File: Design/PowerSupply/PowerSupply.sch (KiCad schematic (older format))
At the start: 14 parts, among them J1 Barrel_Jack, J2 Conn_01x02_Male, Q1 IRF644, U1 MAX1771

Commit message: Add part numbers to symbols in PowerSupply schematic for BOM
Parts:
- C1: Digikey # (none) -> 478-TPSD107M020R0150DKR-ND; Manufacturer (none) -> AVX
- C2, C3: Digikey # (none) -> 1276-1007-6-ND; Manufacturer (none) -> SAMSUNG
- C4: Digikey # (none) -> PCE3432DKR-ND; Manufacturer (none) -> PANASONIC
- D1: Digikey # (none) -> ES2F-E3/52TGIDKR-ND; Manufacturer (none) -> VISHAY
- J1: Digikey # (none) -> 2092-KLDX-0202-A-ND; Manufacturer (none) -> KYCON
- L1: Digikey # (none) -> 513-1526-6-ND; Manufacturer (none) -> EATON
- Q1: Digikey # (none) -> IRF644STRLPBFDKR-ND; Manufacturer (none) -> VISHAY
- R1: Digikey # (none) -> YAG2156DKR-ND; Manufacturer (none) -> YAGEO
- R2: Digikey # (none) -> 311-1.2MERDKR-ND; Manufacturer (none) -> YAGEO
- R3: Digikey # (none) -> 311-10KARDKR-ND; Manufacturer (none) -> YAGEO
- RV1: Digikey # (none) -> 3362P-502LF-ND; Manufacturer (none) -> BOURNS
- U1: Digikey # (none) -> MAX1771CSA+DKR-ND; Manufacturer (none) -> MAXIM
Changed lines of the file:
@@
 F 1 "MAX1771" H 6000 4000 50  0000 C CNN
 F 2 "Package_SO:SOIC-8_3.9x4.9mm_P1.27mm" H 5700 4650 50  0001 C CNN
-F 3 "" H 5700 4650 50  0001 C CNN
+F 3 "MAX1771CSA+T" H 5700 4650 50  0001 C CNN
+F 4 "MAX1771CSA+DKR-ND" H 5700 3650 50  0001 C CNN "Digikey #"
+F 5 "MAXIM" H 5700 3650 50  0001 C CNN "Manufacturer"
 	1    5700 3650
 	1    0    0    -1
@@
 F 1 "100nF" H 5115 4055 50  0000 L CNN
 F 2 "Capacitor_SMD:C_0805_2012Metric" H 5038 3950 50  0001 C CNN
-F 3 "~" H 5000 4100 50  0001 C CNN
+F 3 "CL21F104ZBCNNNC" H 5000 4100 50  0001 C CNN
+F 4 "1276-1007-6-ND" H 5000 4100 50  0001 C CNN "Digikey #"
+F 5 "SAMSUNG" H 5000 4100 50  0001 C CNN "Manufacturer"
 	1    5000 4100
 	1    0    0    -1
@@
 F 1 "IRF644" H 6706 3405 50  0000 L CNN
 F 2 "Package_TO_SOT_SMD:TO-263-2" H 6700 3550 50  0001 C CNN
-F 3 "~" H 6500 3450 50  0001 C CNN
+F 3 "IRF644STRLPBF" H 6500 3450 50  0001 C CNN
+F 4 "IRF644STRLPBFDKR-ND" H 6500 3450 50  0001 C CNN "Digikey #"
+F 5 "VISHAY" H 6500 3450 50  0001 C CNN "Manufacturer"
 	1    6500 3450
 	1    0    0    -1
@@
 F 1 "100uH,2A" V 6449 3150 50  0000 C CNN
 F 2 "Inductor_SMD:L_12x12mm_H4.5mm" H 6350 3150 50  0001 C CNN
-F 3 "~" H 6350 3150 50  0001 C CNN
+F 3 "DR125-101-R" H 6350 3150 50  0001 C CNN
+F 4 "513-1526-6-ND" H 6350 3150 50  0001 C CNN "Digikey #"
+F 5 "EATON" H 6350 3150 50  0001 C CNN "Manufacturer"
 	1    6350 3150
 	0    -1   -1   0
@@
 F 1 "0.05,1W" H 6670 4055 50  0000 L CNN
 F 2 "Resistor_SMD:R_2512_6332Metric" V 6530 4100 50  0001 C CNN
-F 3 "~" H 6600 4100 50  0001 C CNN
+F 3 "PE2512FKE070R05L" H 6600 4100 50  0001 C CNN
+F 4 "YAG2156DKR-ND" H 6600 4100 50  0001 C CNN "Digikey #"
+F 5 "YAGEO" H 6600 4100 50  0001 C CNN "Manufacturer"
 	1    6600 4100
 	1    0    0    -1
@@
 F 2 "Diode_SMD:D_SMB" H 6950 3150 50  0001 C CNN
 F 3 "ES2F-E3/52T" H 6950 3150 50  0001 C CNN
+F 4 "ES2F-E3/52TGIDKR-ND" H 6950 3150 50  0001 C CNN "Digikey #"
+F 5 "VISHAY" H 6950 3150 50  0001 C CNN "Manufacturer"
 	1    6950 3150
 	-1   0    0    1
@@
 F 1 "100nF" H 5015 3305 50  0000 L CNN
 F 2 "Capacitor_SMD:C_0805_2012Metric" H 4938 3200 50  0001 C CNN
-F 3 "~" H 4900 3350 50  0001 C CNN
+F 3 "CL21F104ZBCNNNC" H 4900 3350 50  0001 C CNN
+F 4 "1276-1007-6-ND" H 4900 3350 50  0001 C CNN "Digikey #"
+F 5 "SAMSUNG" H 4900 3350 50  0001 C CNN "Manufacturer"
 	1    4900 3350
 	1    0    0    -1
@@
 F 1 "1M2,250V" H 7420 3555 50  0000 L CNN
 F 2 "Resistor_SMD:R_1206_3216Metric" V 7280 3600 50  0001 C CNN
-F 3 "~" H 7350 3600 50  0001 C CNN
+F 3 "RC1206JR-071M2L" H 7350 3600 50  0001 C CNN
+F 4 "311-1.2MERDKR-ND" H 7350 3600 50  0001 C CNN "Digikey #"
+F 5 "YAGEO" H 7350 3600 50  0001 C CNN "Manufacturer"
 	1    7350 3600
 	1    0    0    -1
@@
 F 1 "10K" H 7420 4055 50  0000 L CNN
 F 2 "Resistor_SMD:R_0805_2012Metric" V 7280 4100 50  0001 C CNN
-F 3 "~" H 7350 4100 50  0001 C CNN
+F 3 "RC0805JR-0710KL" H 7350 4100 50  0001 C CNN
+F 4 "311-10KARDKR-ND" H 7350 4100 50  0001 C CNN "Digikey #"
+F 5 "YAGEO" H 7350 4100 50  0001 C CNN "Manufacturer"
 	1    7350 4100
 	1    0    0    -1
@@
 F 2 "Capacitor_SMD:CP_Elec_10x10" H 7988 3450 50  0001 C CNN
 F 3 "EEV-EB2E100Q" H 7950 3600 50  0001 C CNN
+F 4 "PCE3432DKR-ND" H 7950 3600 50  0001 C CNN "Digikey #"
+F 5 "PANASONIC" H 7950 3600 50  0001 C CNN "Manufacturer"
 	1    7950 3600
 	1    0    0    -1
@@
 F 1 "100uF,Low ESR" H 4168 3305 50  0000 L CNN
 F 2 "Capacitor_Tantalum_SMD:CP_EIA-7343-31_Kemet-D" H 4088 3200 50  0001 C CNN
-F 3 "TPSD107M020R0085" H 4050 3350 50  0001 C CNN
+F 3 "TPSD107M020R0150" H 4050 3350 50  0001 C CNN
+F 4 "	478-TPSD107M020R0150DKR-ND" H 4050 3350 50  0001 C CNN "Digikey #"
+F 5 "AVX" H 4050 3350 50  0001 C CNN "Manufacturer"
 	1    4050 3350
 	1    0    0    -1
@@
 F 1 "10K" V 7144 4400 50  0000 C CNN
 F 2 "Potentiometer_THT:Potentiometer_Bourns_3339P_Vertical" H 7350 4400 50  0001 C CNN
-F 3 "~" H 7350 4400 50  0001 C CNN
+F 3 "3362P-1-502LF" H 7350 4400 50  0001 C CNN
+F 4 "3362P-502LF-ND" H 7350 4400 50  0001 C CNN "Digikey #"
+F 5 "BOURNS" H 7350 4400 50  0001 C CNN "Manufacturer"
 	1    7350 4400
 	0    -1   -1   0
@@
 F 1 "Barrel_Jack" H 2600 5650 50  0000 C CNN
 F 2 "Connector_BarrelJack:BarrelJack_Horizontal" H 2750 5360 50  0001 C CNN
-F 3 "~" H 2750 5360 50  0001 C CNN
+F 3 "KLDX-0202-A" H 2750 5360 50  0001 C CNN
+F 4 "2092-KLDX-0202-A-ND" H 2700 5400 50  0001 C CNN "Digikey #"
+F 5 "KYCON" H 2700 5400 50  0001 C CNN "Manufacturer"
 	1    2700 5400
 	1    0    0    -1
@@
 F 1 "Conn_01x02_Male" H 3850 5500 50  0000 C CNN
 F 2 "Connector_PinHeader_2.54mm:PinHeader_1x02_P2.54mm_Vertical" H 3750 5400 50  0001 C CNN
-F 3 "~" H 3750 5400 50  0001 C CNN
+F 3 "" H 3750 5400 50  0001 C CNN
 	1    3750 5400
 	1    0    0    -1

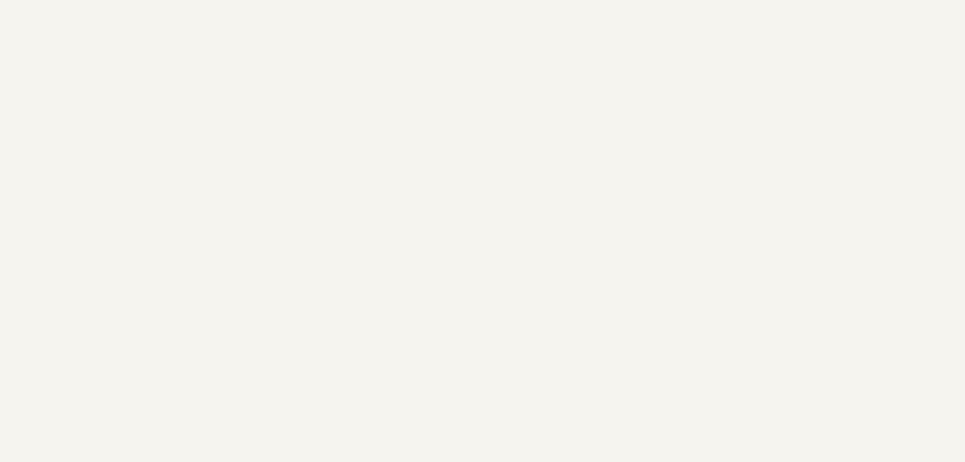
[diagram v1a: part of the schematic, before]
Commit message: Add license notice to all human readable files
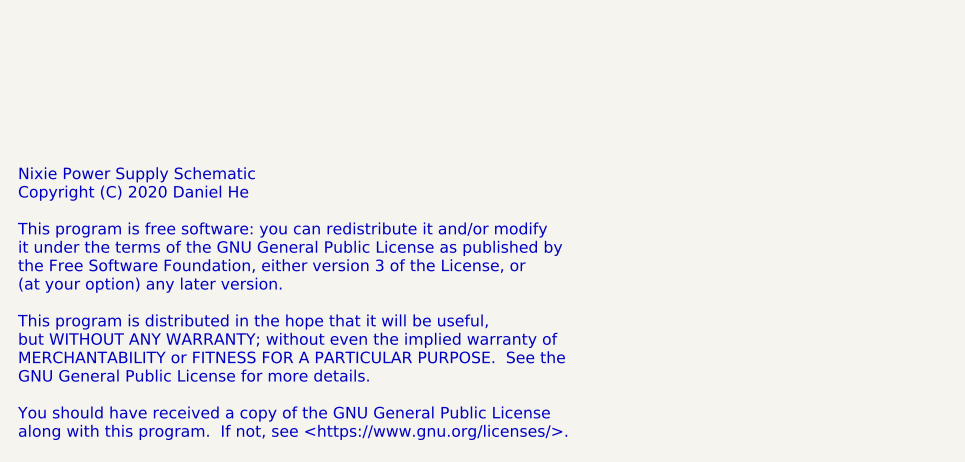
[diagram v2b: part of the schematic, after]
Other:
- note added: "Nixie Power Supply Schematic\nCopyright (C) 2020 Daniel He\n\nThis program is free software: you can redistribute it and/or modify\nit under the terms of the GNU General Public License as published by\nthe Free Software Foundation, either version 3 of the License, or\n(at your option) any later version.\n\nThis program is distributed in the hope that it will be useful,\nbut WITHOUT ANY WARRANTY; 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"
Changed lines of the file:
@@
 	1    0    0    -1
 $EndComp
+Text Notes 550  7700 0    50   ~ 0
+Nixie Power Supply Schematic\nCopyright (C) 2020 Daniel He\n\nThis program is free software: you can redistribute it and/or modify\nit under the terms of the GNU General Public License as published by\nthe Free Software Foundation, either version 3 of the License, or\n(at your option) any later version.\n\nThis program is distributed in the hope that it will be useful,\nbut WITHOUT ANY WARRANTY; without even the implied warranty of\nMERCHANTABILITY or FITNESS FOR A PARTICULAR PURPOSE.  See the\nGNU General Public License for more details.\n\nYou should have received a copy of the GNU General Public License\nalong with this program.  If not, see <https://www.gnu.org/licenses/>.
 $EndSCHEMATC
